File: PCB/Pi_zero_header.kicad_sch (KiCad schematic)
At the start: 95 parts, among them J1 Raspberry_Pi_2_3, J2 USB_C_Receptacle_USB2.0, J3 Screw_Terminal_01x02, J4 Screw_Terminal_01x02, J5 Conn_02x04_Top_Bottom, J6 Conn_01x07, J7 Conn_01x02, J8 Conn_02x03_Top_Bottom, J9 Conn_01x02, SW1 SW_Push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

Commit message: Finally picked inductors
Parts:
- added JP1, JP2, JP3: SolderJumper_2_Open, Jumper:SolderJumper-2_P1.3mm_Open_RoundedPad1.0x1.5mm, symbol Jumper:SolderJumper_2_Open
- added R24: 6k04, Resistor_SMD:R_0402_1005Metric, symbol Device:R
- added R25: 10k5, Resistor_SMD:R_0402_1005Metric, symbol Device:R
- added R26, R27: 5k1, Resistor_SMD:R_0402_1005Metric, symbol Device:R
- L1: footprint Inductor_SMD:L_1008_2520Metric -> Inductor_SMD:L_Vishay_IFSC-1515AH_4x4x1.8mm
- L2, L3: value 1.5u -> 1u; footprint Inductor_SMD:L_1008_2520Metric -> Inductor_SMD:L_Vishay_IFSC-1515AH_4x4x1.8mm
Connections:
- net INT_N is gone; now on net INT_N_PWR: U6.21 (INT_N)
- net CE_N_RPI: now also U1.7 (GPIO5); no longer U1.9 (GPIO7)
- net GND: now also U6.13 (CE_N), R24.2, R25.2, R26.2, R27.2
- net INT_N_PWR: now also U1.6 (GPIO4); no longer U1.8 (GPIO6)
- net MISO_RPi: now also U1.8 (GPIO6); no longer U1.11 (GPIO8)
- net MOSI_RPi: now also U1.9 (GPIO7); no longer U1.12 (GPIO9)
- net SCLK_RPi: now also U1.11 (GPIO8); no longer J6.3 (Pin_3), U1.13 (GPIO10)
- net at J2.A5 (CC1): now also R26.1
- net at J2.B5 (CC2): now also R27.1
- net at U6.20 (PROG): now also JP1.2 (B), JP2.2 (B), JP3.2 (B); no longer R11.1
- removed net CE_N_PWR: U1.6 (GPIO4), U6.13 (CE_N)
- net QON_N_PWR: no longer names the net of U6.12 (QON_N)
- net QON_N_PWR: no longer U1.7 (GPIO5)
- new net: J6.3 (Pin_3), U1.13 (GPIO10)
- new net: JP3.1 (A), R25.1
- new net: JP1.1 (A), R11.1
- new net: JP2.1 (A), R24.1
- no-connect marks 0 -> 31
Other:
- moved on the sheet: C2, C22, C24, C26, C27, C3, C31, C32, C33, C34, C35, C36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

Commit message: Another changes to PCB
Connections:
- net at JP3.1 (A): now also JP1.1 (A), JP2.1 (A), U6.20 (PROG); no longer R25.1
- net at R11.1: now also JP1.2 (B); no longer JP1.1 (A)
- net at R24.1: now also JP2.2 (B); no longer JP2.1 (A)
- new net: JP3.2 (B), R25.1
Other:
- moved on the sheet: JP1, JP2, JP3
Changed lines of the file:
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@@
     )
   )
-  (symbol (lib_id "Jumper:SolderJumper_2_Open") (at 33.02 105.41 0) (unit 1)
+  (symbol (lib_id "Jumper:SolderJumper_2_Open") (at 33.02 105.41 180) (unit 1)
     (in_bom yes) (on_board yes) (dnp no)
     (property "Reference" "JP3" (at 33.02 107.95 0)
@@
     )
   )
-  (symbol (lib_id "Jumper:SolderJumper_2_Open") (at 33.02 87.63 0) (unit 1)
+  (symbol (lib_id "Jumper:SolderJumper_2_Open") (at 33.02 87.63 180) (unit 1)
     (in_bom yes) (on_board yes) (dnp no)
     (property "Reference" "JP1" (at 33.02 90.17 0)
@@
     )
   )
-  (symbol (lib_id "Jumper:SolderJumper_2_Open") (at 33.02 96.52 0) (unit 1)
+  (symbol (lib_id "Jumper:SolderJumper_2_Open") (at 33.02 96.52 180) (unit 1)
     (in_bom yes) (on_board yes) (dnp no)
     (property "Reference" "JP2" (at 33.02 99.06 0)

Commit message: Bruuuuh, me mad...
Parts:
- added JP4: SolderJumper_2_Open, Jumper:SolderJumper-2_P1.3mm_Open_RoundedPad1.0x1.5mm, symbol Jumper:SolderJumper_2_Open
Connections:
- net +3V3: now also JP4.2 (B); no longer C51.1, C52.1, C53.1, R19.1, R21.1, U5.7 (VOUT), U5.8 (VOUT)
- new net: C51.1, C52.1, C53.1, JP4.1 (A), R19.1, R21.1, U5.7 (VOUT), U5.8 (VOUT)
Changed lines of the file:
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@@
     (stroke (width 0) (type default))
   )
+  (wire (pts (xy 140.97 227.33) (xy 140.97 234.95))
+    (stroke (width 0) (type default))
+  )
   (wire (pts (xy 363.22 190.5) (xy 363.22 182.88))
     (stroke (width 0) (type default))
@@
     (stroke (width 0) (type default))
   )
-  (wire (pts (xy 140.97 229.87) (xy 140.97 234.95))
+  (wire (pts (xy 140.97 215.9) (xy 140.97 219.71))
     (stroke (width 0) (type default))
   )
@@
     )
   )
+  (symbol (lib_id "Jumper:SolderJumper_2_Open") (at 140.97 223.52 90) (unit 1)
+    (in_bom yes) (on_board yes) (dnp no)
+    (property "Reference" "JP4" (at 138.43 223.52 0)
+      (effects (font (size 1.27 1.27)))
+    )
+    (property "Value" "SolderJumper_2_Open" (at 135.89 223.52 0)
+      (effects (font (size 1.27 1.27)))
+    )
+    (property "Footprint" "Jumper:SolderJumper-2_P1.3mm_Open_RoundedPad1.0x1.5mm" (at 140.97 223.52 0)
+      (effects (font (size 1.27 1.27)) hide)
+    )
+    (property "Datasheet" "~" (at 140.97 223.52 0)
+      (effects (font (size 1.27 1.27)) hide)
+    )
+    (pin "2")
+    (pin "1")
+    (instances
+      (project "Pi_zero_header"
+        (path "/b619a5d9-7fc7-4364-bf63-192bb5e8977a"
+          (reference "JP4") (unit 1)
+        )
+      )
+    )
+  )
   (symbol (lib_id "Device:C") (at 29.21 167.64 0) (unit 1)
     (in_bom yes) (on_board yes) (dnp no) (fields_autoplaced)
@@
     )
   )
-  (symbol (lib_id "power:+3V3") (at 140.97 229.87 0) (unit 1)
+  (symbol (lib_id "power:+3V3") (at 140.97 215.9 0) (unit 1)
     (in_bom yes) (on_board yes) (dnp no) (fields_autoplaced)
-    (property "Reference" "#PWR055" (at 140.97 233.68 0)
+    (property "Reference" "#PWR055" (at 140.97 219.71 0)
       (effects (font (size 1.27 1.27)) hide)
     )
-    (property "Value" "+3V3" (at 140.97 224.79 0)
+    (property "Value" "+3V3" (at 140.97 210.82 0)
       (effects (font (size 1.27 1.27)))
     )
-    (property "Footprint" "" (at 140.97 229.87 0)
+    (property "Footprint" "" (at 140.97 215.9 0)
       (effects (font (size 1.27 1.27)) hide)
     )
-    (property "Datasheet" "" (at 140.97 229.87 0)
+    (property "Datasheet" "" (at 140.97 215.9 0)
       (effects (font (size 1.27 1.27)) hide)
     )

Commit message: Another commit :)
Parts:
- removed C4, C48: 10u, Capacitor_SMD:C_0805_2012Metric, symbol Device:C
- removed C44, C52: 22u, Capacitor_SMD:C_0805_2012Metric, symbol Device:C
- C41, C47: value 10u -> 22u
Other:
- moved on the sheet: C41, C45, C47, C53, JP4, R17, R20

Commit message: Bruh, I forgor...
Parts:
- removed J3, J4: Screw_Terminal_01x02, TerminalBlock_TE-Connectivity:TerminalBlock_TE_282834-2_1x02_P2.54mm_Horizontal, symbol Connector:Screw_Terminal_01x02
- added J3, J4: Conn_01x02, Connector_PinHeader_2.54mm:PinHeader_1x02_P2.54mm_Vertical, symbol Connector_Generic:Conn_01x02
- J2: footprint Connector_USB:USB_C_Receptacle_GCT_USB4105-xx-A_16P_TopMnt_Horizontal -> Connector_USB:USB_C_Receptacle_GCT_USB4110
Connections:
- net at U3.11 (BO1), U3.12 (BO1): now also J4.1 (Pin_1)
- net at U3.7 (BO2), U3.8 (BO2): now also J4.2 (Pin_2)
- net at U3.1 (AO1), U3.2 (AO1): now also J3.1 (Pin_1)
- net at U3.5 (AO2), U3.6 (AO2): now also J3.2 (Pin_2)
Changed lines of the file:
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@@
+    )
+  )
+  (symbol (lib_id "Connector_Generic:Conn_01x02") (at 388.62 220.98 0) (unit 1)
+    (in_bom yes) (on_board yes) (dnp no) (fields_autoplaced)
+    (property "Reference" "J4" (at 391.16 220.98 0)
+      (effects (font (size 1.27 1.27)) (justify left))
+    )
+    (property "Value" "Conn_01x02" (at 391.16 223.52 0)
+      (effects (font (size 1.27 1.27)) (justify left))
+    )
+    (property "Footprint" "Connector_PinHeader_2.54mm:PinHeader_1x02_P2.54mm_Vertical" (at 388.62 220.98 0)
+      (effects (font (size 1.27 1.27)) hide)
+    )
+    (property "Datasheet" "~" (at 388.62 220.98 0)
+      (effects (font (size 1.27 1.27)) hide)
+    )
+    (pin "1")
+    (pin "2")
+    (instances
+      (project "Pi_zero_header"
+        (path "/b619a5d9-7fc7-4364-bf63-192bb5e8977a"
+          (reference "J4") (unit 1)
+        )
+      )
     )
   )
@@
     )
   )
-  (symbol (lib_id "Connector:Screw_Terminal_01x02") (at 388.62 220.98 0) (unit 1)
-    (in_bom yes) (on_board yes) (dnp no)
-    (property "Reference" "J4" (at 387.35 226.06 0)
-      (effects (font (size 1.27 1.27)) (justify left))
-    )
-    (property "Value" "Screw_Terminal_01x02" (at 378.46 228.6 0)
-      (effects (font (size 1.27 1.27)) (justify left))
-    )
-    (property "Footprint" "TerminalBlock_TE-Connectivity:TerminalBlock_TE_282834-2_1x02_P2.54mm_Horizontal" (at 388.62 220.98 0)
-      (effects (font (size 1.27 1.27)) hide)
-    )
-    (property "Datasheet" "~" (at 388.62 220.98 0)
-      (effects (font (size 1.27 1.27)) hide)
-    )
-    (pin "1")
-    (pin "2")
-    (instances
-      (project "Pi_zero_header"
-        (path "/b619a5d9-7fc7-4364-bf63-192bb5e8977a"
-          (reference "J4") (unit 1)
-        )
-      )
-    )
-  )
   (symbol (lib_id "Device:C") (at 153.67 67.31 0) (mirror y) (unit 1)
     (in_bom yes) (on_board yes) (dnp no) (fields_autoplaced)
@@
       (effects (font (size 1.27 1.27)))
     )
-    (property "Footprint" "Connector_USB:USB_C_Receptacle_GCT_USB4105-xx-A_16P_TopMnt_Horizontal" (at 207.01 52.07 0)
+    (property "Footprint" "Connector_USB:USB_C_Receptacle_GCT_USB4110" (at 207.01 52.07 0)
       (effects (font (size 1.27 1.27)) hide)
     )
@@
     )
   )
-  (symbol (lib_id "Connector:Screw_Terminal_01x02") (at 388.62 208.28 0) (unit 1)
-    (in_bom yes) (on_board yes) (dnp no)
-    (property "Reference" "J3" (at 387.35 213.36 0)
-      (effects (font (size 1.27 1.27)) (justify left))
-    )
-    (property "Value" "Screw_Terminal_01x02" (at 378.46 215.9 0)
-      (effects (font (size 1.27 1.27)) (justify left))
-    )
-    (property "Footprint" "TerminalBlock_TE-Connectivity:TerminalBlock_TE_282834-2_1x02_P2.54mm_Horizontal" (at 388.62 208.28 0)
-      (effects (font (size 1.27 1.27)) hide)
-    )
-    (property "Datasheet" "~" (at 388.62 208.28 0)
-      (effects (font (size 1.27 1.27)) hide)
-    )
-    (pin "1")
-    (pin "2")
-    (instances
-      (project "Pi_zero_header"
-        (path "/b619a5d9-7fc7-4364-bf63-192bb5e8977a"
-          (reference "J3") (unit 1)
-        )
-      )
-    )
-  )
   (symbol (lib_id "power:+BATT") (at 261.62 255.27 0) (unit 1)
     (in_bom yes) (on_board yes) (dnp no) (fields_autoplaced)
@@
         )
       )
+    )
+  )
+  (symbol (lib_id "Connector_Generic:Conn_01x02") (at 388.62 208.28 0) (unit 1)
+    (in_bom yes) (on_board yes) (dnp no) (fields_autoplaced)
+    (property "Reference" "J3" (at 391.16 208.28 0)
+      (effects (font (size 1.27 1.27)) (justify left))
+    )
+    (property "Value" "Conn_01x02" (at 391.16 210.82 0)
+      (effects (font (size 1.27 1.27)) (justify left))
+    )
+    (property "Footprint" "Connector_PinHeader_2.54mm:PinHeader_1x02_P2.54mm_Vertical" (at 388.62 208.28 0)
+      (effects (font (size 1.27 1.27)) hide)
+    )
+    (property "Datasheet" "~" (at 388.62 208.28 0)
+      (effects (font (size 1.27 1.27)) hide)
+    )
+    (pin "1")
+    (pin "2")
+    (instances
+      (project "Pi_zero_header"
+        (path "/b619a5d9-7fc7-4364-bf63-192bb5e8977a"
+          (reference "J3") (unit 1)
+        )
+      )

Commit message: Finally gonna rout'em
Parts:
- removed J5: Conn_02x04_Top_Bottom, Connector_PinHeader_2.54mm:PinHeader_2x04_P2.54mm_Vertical, symbol Connector_Generic:Conn_02x04_Top_Bottom
- added J5: Conn_02x04_Odd_Even, Connector_PinHeader_2.54mm:PinHeader_2x04_P2.54mm_Vertical, symbol Connector_Generic:Conn_02x04_Odd_Even
- J8: symbol Connector_Generic:Conn_02x03_Top_Bottom -> Connector_Generic:Conn_02x03_Odd_Even
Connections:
- net +3V3: now also J5.1 (Pin_1), J5.2 (Pin_2)
- net +5V: now also J8.3 (Pin_3), J8.4 (Pin_4); no longer J8.2 (Pin_2), J8.5 (Pin_5)
- net GND: now also J8.5 (Pin_5), J5.3 (Pin_3), J5.4 (Pin_4); no longer J8.3 (Pin_3)
- net at U1.18 (GPIO15): now also J8.2 (Pin_2); no longer J8.4 (Pin_4)
- net at U1.2 (GPIO0): now also J5.5 (Pin_5), J5.6 (Pin_6)
- net at U1.3 (GPIO1): now also J5.7 (Pin_7), J5.8 (Pin_8)
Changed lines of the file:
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@@
-    )
-  )
-  (symbol (lib_id "Connector_Generic:Conn_02x04_Top_Bottom") (at 375.92 66.04 0) (unit 1)
-    (in_bom yes) (on_board yes) (dnp no) (fields_autoplaced)
-    (property "Reference" "J5" (at 377.19 57.15 0)
-      (effects (font (size 1.27 1.27)))
-    )
-    (property "Value" "Conn_02x04_Top_Bottom" (at 377.19 59.69 0)
-      (effects (font (size 1.27 1.27)))
-    )
-    (property "Footprint" "Connector_PinHeader_2.54mm:PinHeader_2x04_P2.54mm_Vertical" (at 375.92 66.04 0)
-      (effects (font (size 1.27 1.27)) hide)
-    )
-    (property "Datasheet" "~" (at 375.92 66.04 0)
-      (effects (font (size 1.27 1.27)) hide)
-    )
-    (pin "8")
-    (pin "7")
-    (pin "6")
-    (pin "2")
-    (pin "3")
-    (pin "5")
-    (pin "4")
-    (pin "1")
-    (instances
-      (project "Pi_zero_header"
-        (path "/b619a5d9-7fc7-4364-bf63-192bb5e8977a"
-          (reference "J5") (unit 1)
-        )
-      )
     )
   )
@@
     )
   )
-  (symbol (lib_id "Connector_Generic:Conn_02x03_Top_Bottom") (at 383.54 142.24 0) (unit 1)
+  (symbol (lib_id "Connector_Generic:Conn_02x03_Odd_Even") (at 383.54 142.24 0) (unit 1)
     (in_bom yes) (on_board yes) (dnp no) (fields_autoplaced)
     (property "Reference" "J8" (at 384.81 133.35 0)
@@
         )
       )
+    )
+  )
+  (symbol (lib_id "Connector_Generic:Conn_02x04_Odd_Even") (at 375.92 66.04 0) (unit 1)
+    (in_bom yes) (on_board yes) (dnp no) (fields_autoplaced)
+    (property "Reference" "J5" (at 377.19 57.15 0)
+      (effects (font (size 1.27 1.27)))
+    )
+    (property "Value" "Conn_02x04_Odd_Even" (at 377.19 59.69 0)
+      (effects (font (size 1.27 1.27)))
+    )
+    (property "Footprint" "Connector_PinHeader_2.54mm:PinHeader_2x04_P2.54mm_Vertical" (at 375.92 66.04 0)
+      (effects (font (size 1.27 1.27)) hide)
+    )
+    (property "Datasheet" "~" (at 375.92 66.04 0)
+      (effects (font (size 1.27 1.27)) hide)
+    )
+    (pin "7")
+    (pin "2")
+    (pin "5")
+    (pin "6")
+    (pin "3")
+    (pin "4")
+    (pin "1")
+    (pin "8")
+    (instances
+      (project "Pi_zero_header"
+        (path "/b619a5d9-7fc7-4364-bf63-192bb5e8977a"
+          (reference "J5") (unit 1)
+        )
+      )

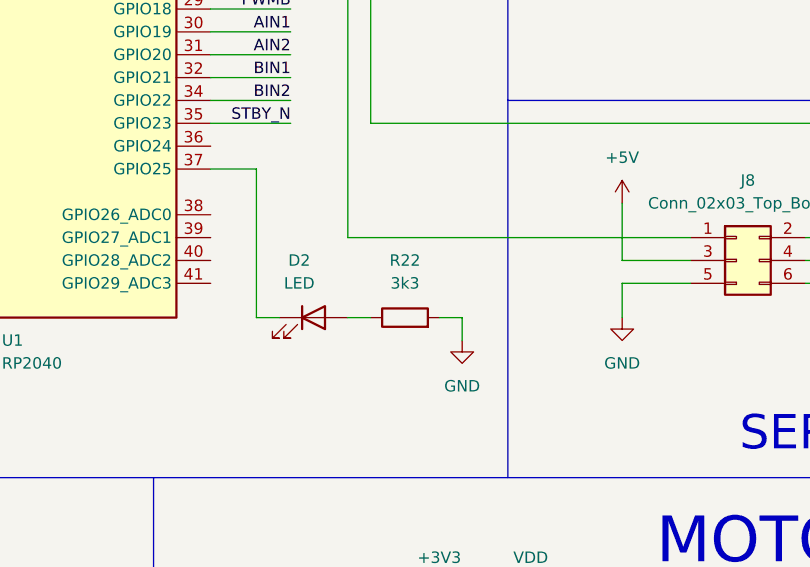
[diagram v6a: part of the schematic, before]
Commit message: Changed connectors
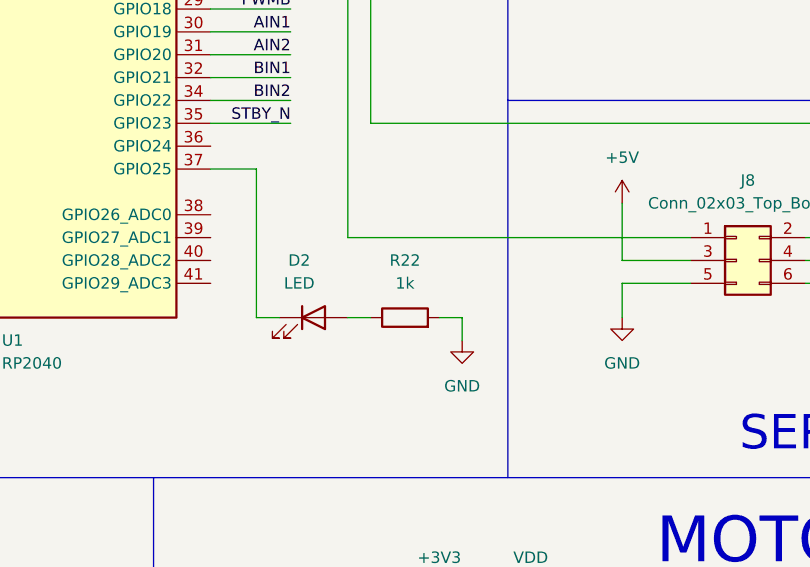
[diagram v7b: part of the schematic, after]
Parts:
- D1, D2: footprint LED_SMD:LED_0402_1005Metric -> LED_SMD:LED_0603_1608Metric
- J5: footprint Connector_PinHeader_2.54mm:PinHeader_2x04_P2.54mm_Vertical -> Connector_PinHeader_1.27mm:PinHeader_2x04_P1.27mm_Vertical
- J6: footprint Connector_PinHeader_2.54mm:PinHeader_1x07_P2.54mm_Vertical -> Connector_PinHeader_1.27mm:PinHeader_1x07_P1.27mm_Vertical
- R22: value 3k3 -> 1k
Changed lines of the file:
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@@
       (effects (font (size 1.27 1.27)))
     )
-    (property "Value" "3k3" (at 346.71 144.78 90)
+    (property "Value" "1k" (at 346.71 144.78 90)
       (effects (font (size 1.27 1.27)))
     )
@@
       (effects (font (size 1.27 1.27)))
     )
-    (property "Footprint" "LED_SMD:LED_0402_1005Metric" (at 128.27 96.52 0)
+    (property "Footprint" "LED_SMD:LED_0603_1608Metric" (at 128.27 96.52 0)
       (effects (font (size 1.27 1.27)) hide)
     )
@@
       (effects (font (size 1.27 1.27)))
     )
-    (property "Footprint" "LED_SMD:LED_0402_1005Metric" (at 336.55 148.59 0)
+    (property "Footprint" "LED_SMD:LED_0603_1608Metric" (at 336.55 148.59 0)
       (effects (font (size 1.27 1.27)) hide)
     )
@@
       (effects (font (size 1.27 1.27)))
     )
-    (property "Footprint" "Connector_PinHeader_2.54mm:PinHeader_2x04_P2.54mm_Vertical" (at 375.92 66.04 0)
+    (property "Footprint" "Connector_PinHeader_1.27mm:PinHeader_2x04_P1.27mm_Vertical" (at 375.92 66.04 0)
       (effects (font (size 1.27 1.27)) hide)
     )
@@
       (effects (font (size 1.27 1.27)) (justify left))
     )
-    (property "Footprint" "Connector_PinHeader_2.54mm:PinHeader_1x07_P2.54mm_Vertical" (at 382.27 96.52 0)
+    (property "Footprint" "Connector_PinHeader_1.27mm:PinHeader_1x07_P1.27mm_Vertical" (at 382.27 96.52 0)
       (effects (font (size 1.27 1.27)) hide)
     )

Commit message: Making changes...
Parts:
- removed J5: Conn_02x04_Odd_Even, Connector_PinHeader_1.27mm:PinHeader_2x04_P1.27mm_Vertical, symbol Connector_Generic:Conn_02x04_Odd_Even
- added J10, J11, J12, J5: Conn_01x04, Connector_PinHeader_1.27mm:PinHeader_1x04_P1.27mm_Vertical, symbol Connector_Generic:Conn_01x04
- added J13: Conn_01x07, Connector_PinHeader_1.27mm:PinHeader_1x07_P1.27mm_Vertical, symbol Connector_Generic:Conn_01x07
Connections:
- net +3V3: now also J10.1 (Pin_1), J11.1 (Pin_1), J12.1 (Pin_1), J13.1 (Pin_1), J5.1 (Pin_1)
- net AIN1: now also U1.4 (GPIO2); no longer U1.30 (GPIO19)
- net AIN2: now also U1.3 (GPIO1); no longer U1.31 (GPIO20)
- net BIN1: now also U1.6 (GPIO4); no longer U1.32 (GPIO21)
- net BIN2: now also U1.7 (GPIO5); no longer U1.34 (GPIO22)
- net CE_N_RPI: now also U1.34 (GPIO22); no longer U1.7 (GPIO5)
- net GND: now also J10.2 (Pin_2), J11.2 (Pin_2), J12.2 (Pin_2), J13.2 (Pin_2), J5.2 (Pin_2)
- net INT_N_PWR: no longer U1.6 (GPIO4)
- net MISO_RPi: now also U1.35 (GPIO23); no longer U1.8 (GPIO6)
- net MOSI_RPi: now also U1.36 (GPIO24); no longer U1.9 (GPIO7)
- net PWMA: now also U1.2 (GPIO0); no longer U1.28 (GPIO17)
- net PWMB: now also U1.8 (GPIO6); no longer U1.29 (GPIO18)
- net SCLK_RPi: now also U1.37 (GPIO25); no longer U1.11 (GPIO8)
- net SCL_PWR: no longer U1.4 (GPIO2)
- net SDA_PWR: no longer U1.5 (GPIO3)
- net STBY_N: now also U1.5 (GPIO3); no longer U1.35 (GPIO23)
- net at U1.13 (GPIO10): no longer J6.3 (Pin_3)
- net at U1.14 (GPIO11): no longer J6.4 (Pin_4)
- net at U1.15 (GPIO12): no longer J6.5 (Pin_5)
- net at U1.16 (GPIO13): no longer J6.6 (Pin_6)
- net at U1.17 (GPIO14): no longer J6.7 (Pin_7)
- net at U1.18 (GPIO15): no longer J8.2 (Pin_2)
- net at U1.27 (GPIO16): no longer J8.1 (Pin_1)
- net at D2.1 (K): no longer U1.37 (GPIO25)
- new net: J10.3 (Pin_3), J11.3 (Pin_3), J12.3 (Pin_3), J5.3 (Pin_3)
- new net: J10.4 (Pin_4), J11.4 (Pin_4), J12.4 (Pin_4), J5.4 (Pin_4)
- new net: J13.3 (Pin_3), J6.3 (Pin_3)
- new net: J13.4 (Pin_4), J6.4 (Pin_4)
- new net: J13.5 (Pin_5), J6.5 (Pin_5)
- new net: J13.6 (Pin_6), J6.6 (Pin_6)
- new net: J13.7 (Pin_7), J6.7 (Pin_7)
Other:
- moved on the sheet: J6, R23, R9
